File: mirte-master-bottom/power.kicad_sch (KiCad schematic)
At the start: 50 parts, among them J10 charger, J11 Ext 12v out, J12 USB_A, J18 Conn_01x02_Pin, J19 5V, J2 5vConverter, J20 12V, J21 3V3, J22 switch, J3 battery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

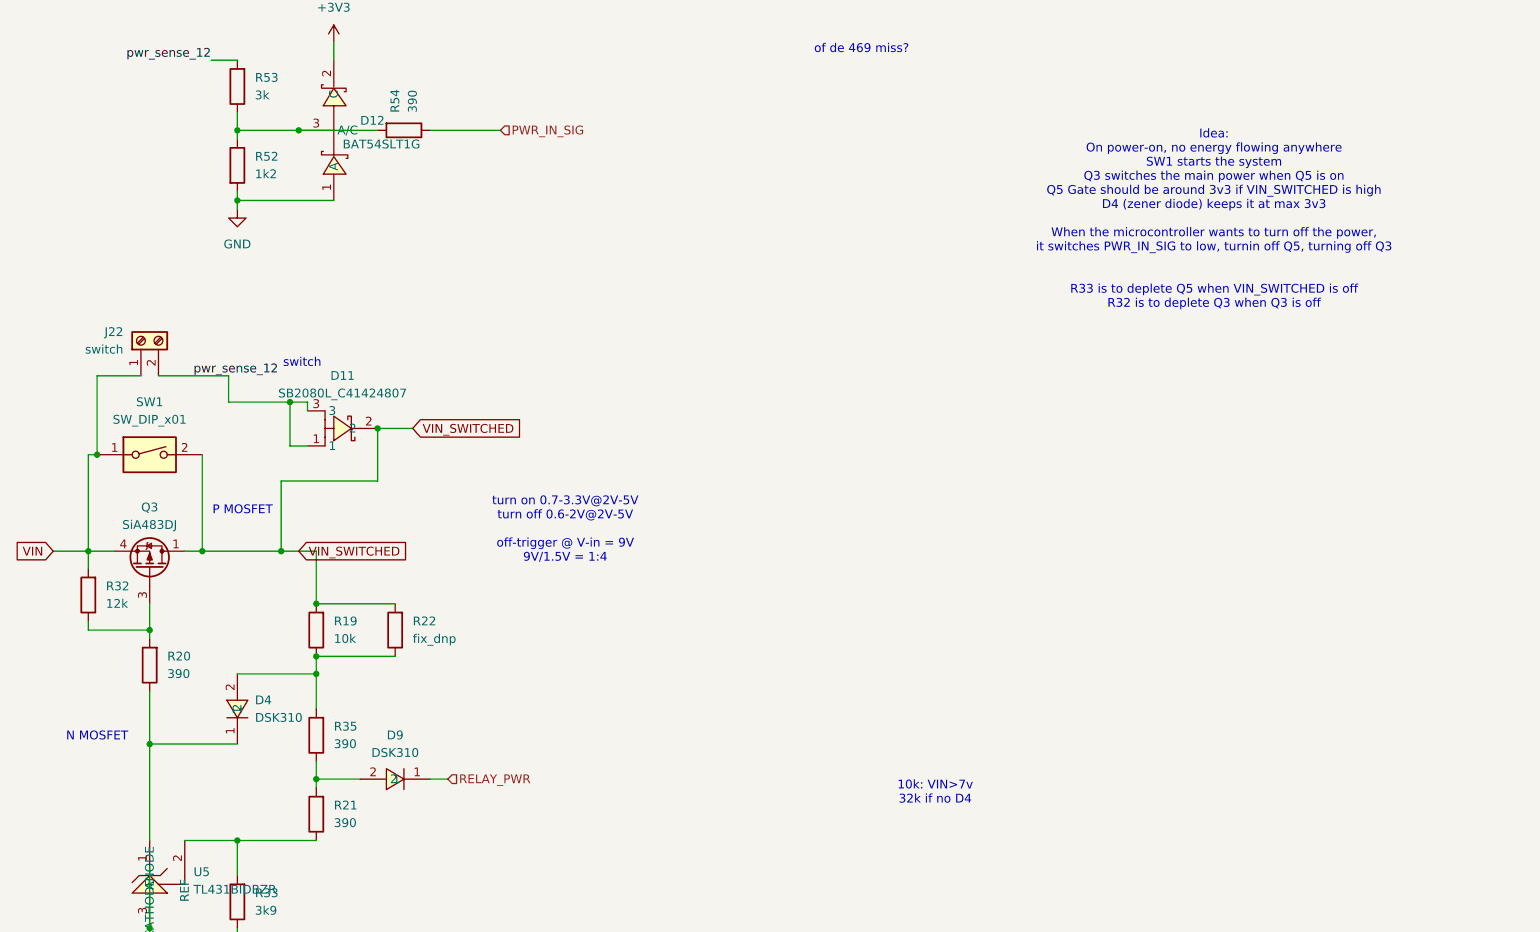
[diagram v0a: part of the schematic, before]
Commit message: Allow mini560 pro for 5v converter MM
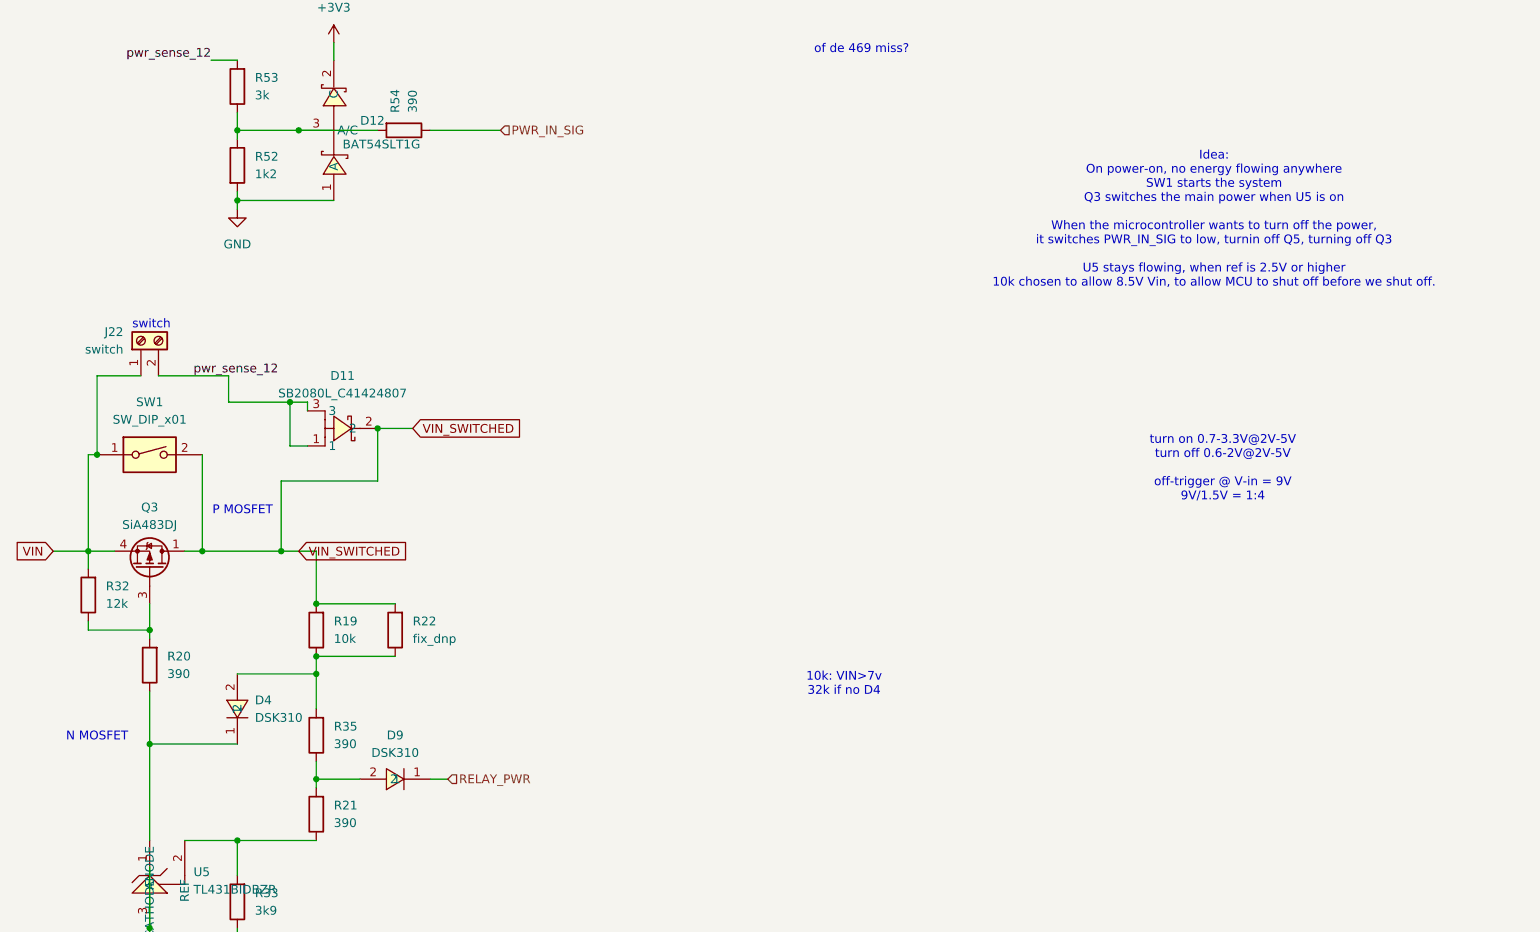
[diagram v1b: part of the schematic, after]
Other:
- note added: "Idea: On power-on, no energy flowing anywhere SW1 starts the system Q3 switches the main power when U5 is on When the microcontroller wants to turn off the power, it switches PWR_IN_SIG to low, turnin off Q5, turning off Q3 U5 stays flowing, when ref is 2.5V or higher 10k chosen to allow 8.5V Vin, to allow MCU to shut off before we shut off."
- note removed: "Idea: On power-on, no energy flowing anywhere SW1 starts the system Q3 switches the main power when Q5 is on Q5 Gate should be around 3v3 if VIN_SWITCHED is high D4 (zener diode) keeps it at max 3v3 When the microcontroller wants to turn off the power, it switches PWR_IN_SIG to low, turnin off Q5, turning off Q3 R33 is to deplete Q5 when VIN_SWITCHED is off R32 is to deplete Q3 when Q3 is off"
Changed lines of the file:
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@@
 	(text "10k: VIN>7v\n32k if no D4"
 		(exclude_from_sim no)
-		(at 447.802 111.252 0)
+		(at 434.594 95.504 0)
 		(effects
 			(font
@@
 		)
 	)
-	(text "Idea:\nOn power-on, no energy flowing anywhere\nSW1 starts the system\nQ3 switches the main power when Q5 is on\nQ5 Gate should be around 3v3 if VIN_SWITCHED is high\nD4 (zener diode) keeps it at max 3v3\n\nWhen the microcontroller wants to turn off the power, \nit switches PWR_IN_SIG to low, turnin off Q5, turning off Q3\n\n\nR33 is to deplete Q5 when VIN_SWITCHED is off\nR32 is to deplete Q3 when Q3 is off"
+	(text "Idea:\nOn power-on, no energy flowing anywhere\nSW1 starts the system\nQ3 switches the main power when U5 is on\n\nWhen the microcontroller wants to turn off the power, \nit switches PWR_IN_SIG to low, turnin off Q5, turning off Q3\n\nU5 stays flowing, when ref is 2.5V or higher\n10k chosen to allow 8.5V Vin, to allow MCU to shut off before we shut off.\n"
 		(exclude_from_sim no)
 		(at 488.188 28.194 0)
@@
 	(text "turn on 0.7-3.3V@2V-5V\nturn off 0.6-2V@2V-5V\n\noff-trigger @ V-in = 9V\n9V/1.5V = 1:4\n"
 		(exclude_from_sim no)
-		(at 394.208 73.152 0)
+		(at 489.458 64.262 0)
 		(effects
 			(font
@@
 	(text "switch"
 		(exclude_from_sim no)
-		(at 356.108 49.022 0)
+		(at 334.264 43.434 0)
 		(effects
 			(font
